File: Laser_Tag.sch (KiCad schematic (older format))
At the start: 16 parts

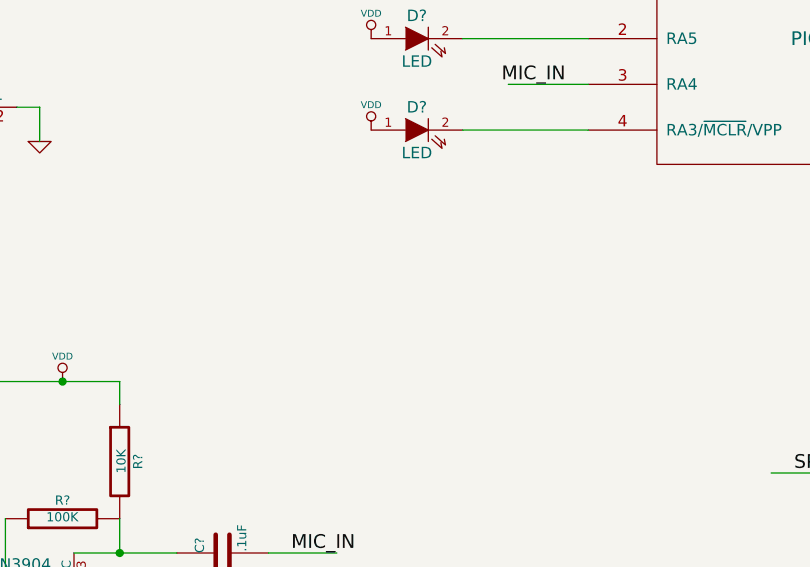
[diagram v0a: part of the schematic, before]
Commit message: Added switch
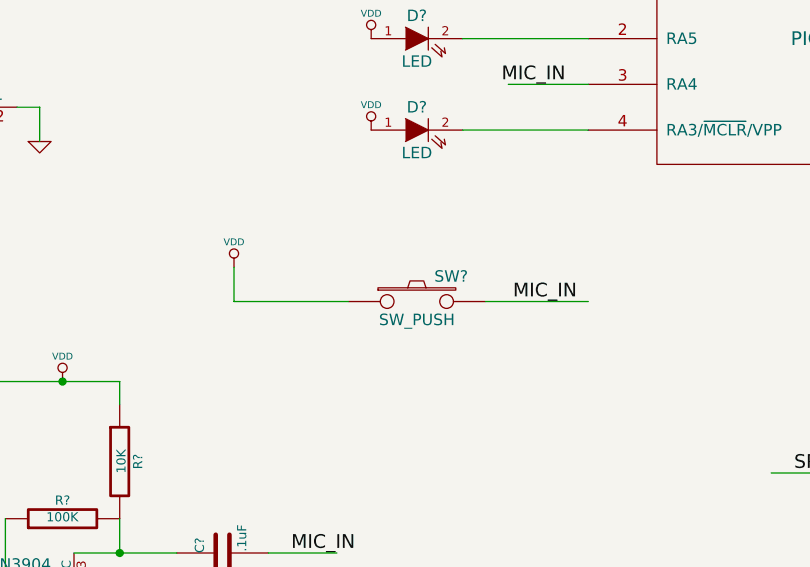
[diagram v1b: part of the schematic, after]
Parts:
- added SW?: SW_PUSH, ~, symbol SW_PUSH
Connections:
- wire segments 33 -> 36
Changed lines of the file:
@@
 LIBS:valves
 LIBS:Banks_custom
+LIBS:Laser_Tag-cache
 EELAYER 27 0
 EELAYER END
@@
 Wire Wire Line
 	2950 3800 2950 3650
+$Comp
+L SW_PUSH SW?
+U 1 1 53D548CF
+P 5400 4650
+F 0 "SW?" H 5550 4760 50  0000 C CNN
+F 1 "SW_PUSH" H 5400 4570 50  0000 C CNN
+F 2 "~" H 5400 4650 60  0000 C CNN
+F 3 "~" H 5400 4650 60  0000 C CNN
+	1    5400 4650
+	1    0    0    -1
+$EndComp
+Wire Wire Line
+	5100 4650 4600 4650
+Wire Wire Line
+	5700 4650 6150 4650
+Text Label 6100 4650 2    60   ~ 0
+MIC_IN
+$Comp
+L VDD #PWR?
+U 1 1 53D5492C
+P 4600 4500
+F 0 "#PWR?" H 4600 4600 30  0001 C CNN
+F 1 "VDD" H 4600 4610 30  0000 C CNN
+F 2 "" H 4600 4500 60  0000 C CNN
+F 3 "" H 4600 4500 60  0000 C CNN
+	1    4600 4500
+	1    0    0    -1
+$EndComp
+Wire Wire Line
+	4600 4650 4600 4500
 $EndSCHEMATC

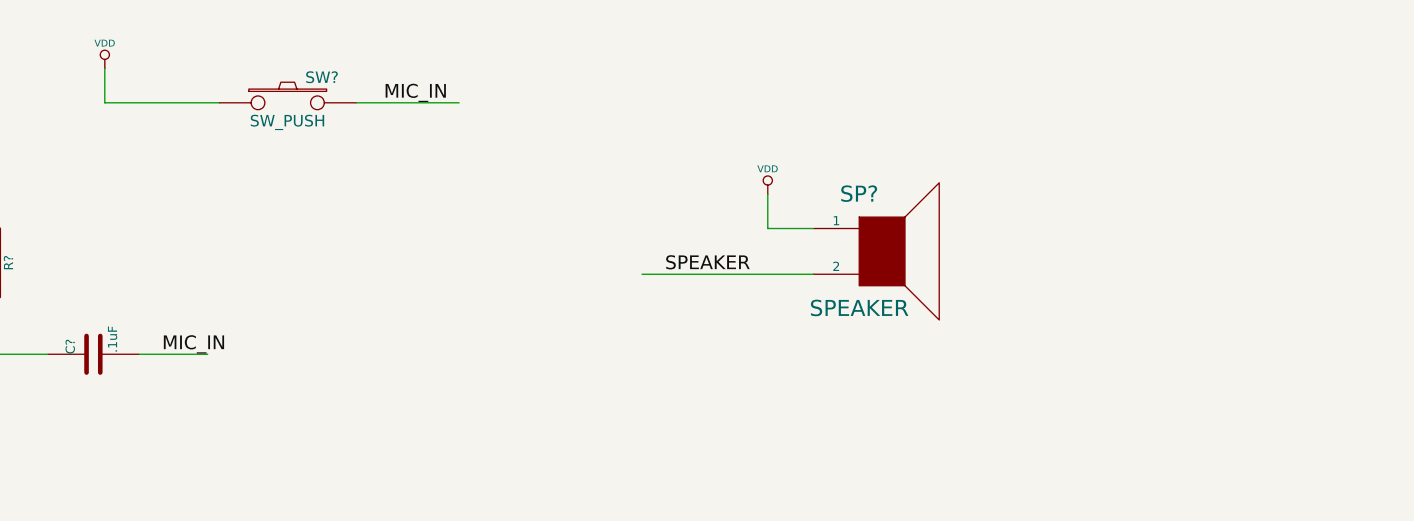
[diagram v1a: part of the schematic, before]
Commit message: Added envelope follow
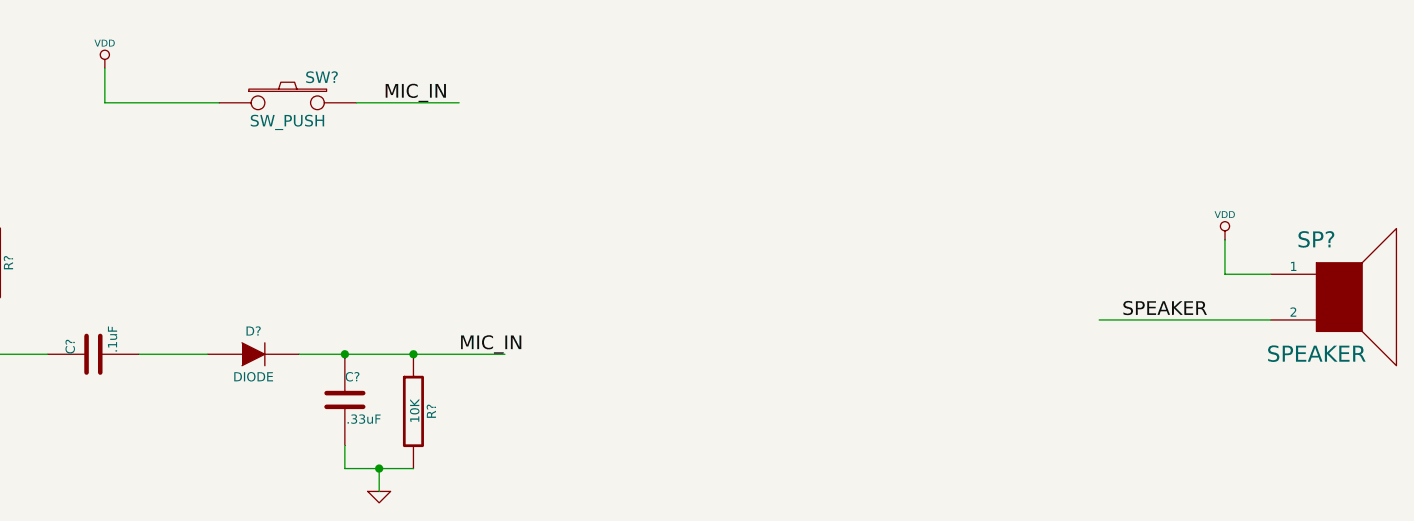
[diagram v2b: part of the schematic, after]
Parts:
- added C?: .33uF, ~, symbol C
- added D?: DIODE, ~, symbol DIODE
- added R?: 10K, ~, symbol R
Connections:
- wire segments 36 -> 40
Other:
- moved on the sheet: SP?
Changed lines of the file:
@@
 L SPEAKER SP?
 U 1 1 53D52F16
-P 8000 5300
-F 0 "SP?" H 7900 5550 70  0000 C CNN
-F 1 "SPEAKER" H 7900 5050 70  0000 C CNN
-F 2 "~" H 8000 5300 60  0000 C CNN
-F 3 "~" H 8000 5300 60  0000 C CNN
-	1    8000 5300
+P 10000 5500
+F 0 "SP?" H 9900 5750 70  0000 C CNN
+F 1 "SPEAKER" H 9900 5250 70  0000 C CNN
+F 2 "~" H 10000 5500 60  0000 C CNN
+F 3 "~" H 10000 5500 60  0000 C CNN
+	1    10000 5500
 	1    0    0    -1
 $EndComp
@@
 	0    -1   -1   0
 $EndComp
-Text Label 4850 5750 0    60   ~ 0
+Text Label 6150 5750 0    60   ~ 0
 MIC_IN
 $Comp
@@
 	1    0    0    -1
 $EndComp
-Text Label 7050 5400 0    60   ~ 0
+Text Label 9050 5600 0    60   ~ 0
 SPEAKER
 $Comp
@@
 	8550 3300 8550 3350
 Wire Wire Line
-	6950 5400 7700 5400
+	8950 5600 9700 5600
 Wire Wire Line
 	6150 3700 5800 3700
@@
 L VDD #PWR?
 U 1 1 53D53BD1
-P 7500 5050
-F 0 "#PWR?" H 7500 5150 30  0001 C CNN
-F 1 "VDD" H 7500 5160 30  0000 C CNN
-F 2 "" H 7500 5050 60  0000 C CNN
-F 3 "" H 7500 5050 60  0000 C CNN
-	1    7500 5050
-	1    0    0    -1
-$EndComp
-Wire Wire Line
-	7500 5050 7500 5200
-Wire Wire Line
-	7500 5200 7700 5200
+P 9500 5250
+F 0 "#PWR?" H 9500 5350 30  0001 C CNN
+F 1 "VDD" H 9500 5360 30  0000 C CNN
+F 2 "" H 9500 5250 60  0000 C CNN
+F 3 "" H 9500 5250 60  0000 C CNN
+	1    9500 5250
+	1    0    0    -1
+$EndComp
+Wire Wire Line
+	9500 5250 9500 5400
+Wire Wire Line
+	9500 5400 9700 5400
 $Comp
 L LED D?
@@
 Wire Wire Line
 	4600 4650 4600 4500
+$Comp
+L DIODE D?
+U 1 1 53D54A1B
+P 5250 5750
+F 0 "D?" H 5250 5850 40  0000 C CNN
+F 1 "DIODE" H 5250 5650 40  0000 C CNN
+F 2 "~" H 5250 5750 60  0000 C CNN
+F 3 "~" H 5250 5750 60  0000 C CNN
+	1    5250 5750
+	1    0    0    -1
+$EndComp
+$Comp
+L C C?
+U 1 1 53D54A2A
+P 5650 5950
+F 0 "C?" H 5650 6050 40  0000 L CNN
+F 1 ".33uF" H 5656 5865 40  0000 L CNN
+F 2 "~" H 5688 5800 30  0000 C CNN
+F 3 "~" H 5650 5950 60  0000 C CNN
+	1    5650 5950
+	1    0    0    -1
+$EndComp
+$Comp
+L R R?
+U 1 1 53D54A39
+P 5950 6000
+F 0 "R?" V 6030 6000 40  0000 C CNN
+F 1 "10K" V 5957 6001 40  0000 C CNN
+F 2 "~" V 5880 6000 30  0000 C CNN
+F 3 "~" H 5950 6000 30  0000 C CNN
+	1    5950 6000
+	1    0    0    -1
+$EndComp
+Wire Wire Line
+	5450 5750 6350 5750
+Connection ~ 5650 5750
+Wire Wire Line
+	5650 6150 5650 6250
+Wire Wire Line
+	5650 6250 5950 6250
+$Comp
+L GND #PWR?
+U 1 1 53D54AC4
+P 5800 6350
+F 0 "#PWR?" H 5800 6350 30  0001 C CNN
+F 1 "GND" H 5800 6280 30  0001 C CNN
+F 2 "" H 5800 6350 60  0000 C CNN
+F 3 "" H 5800 6350 60  0000 C CNN
+	1    5800 6350
+	1    0    0    -1
+$EndComp
+Wire Wire Line
+	5800 6250 5800 6350
+Connection ~ 5800 6250
+Connection ~ 5950 5750
 $EndSCHEMATC

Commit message: Finished board layout
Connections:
- wire segments 40 -> 46
